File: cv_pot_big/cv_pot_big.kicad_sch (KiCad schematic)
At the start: 12 parts, among them J1 I/O connector, U1 HT7550-1, U2 LMV321IDBVR

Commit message: Switched to TLV6001UIDBVR Opamp
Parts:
- RV1: footprint cycfi_library:bourns_pdb181 -> cycfi_library:bourns_pdb241
- U2: value LMV321IDBVR -> TLV6001UIDBVR; LCSC C7972 -> (none)
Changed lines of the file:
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@@
       (effects (font (size 1.27 1.27)) (justify right))
     )
-    (property "Footprint" "cycfi_library:bourns_pdb181" (id 2) (at 88.9 101.6 0)
+    (property "Footprint" "cycfi_library:bourns_pdb241" (id 2) (at 88.9 101.6 0)
       (effects (font (size 1.27 1.27)) hide)
     )
@@
     (in_bom yes) (on_board yes)
     (property "Reference" "U2" (id 0) (at 153.67 96.52 0))
-    (property "Value" "LMV321IDBVR" (id 1) (at 153.67 99.0569 0))
+    (property "Value" "TLV6001UIDBVR" (id 1) (at 153.67 99.0569 0))
     (property "Footprint" "Package_TO_SOT_SMD:SOT-23-5" (id 2) (at 142.24 109.22 0)
       (effects (font (size 1.27 1.27)) (justify left) hide)
@@
     (property "Datasheet" "" (id 3) (at 144.78 99.06 0)
       (effects (font (size 1.27 1.27)) hide)
-    )
-    (property "LCSC" "C7972" (id 4) (at 144.78 104.14 0)
-      (effects (font (size 1.524 1.524)) hide)
     )
     (pin "2")
@@
     )
     (path "/9763309a-c9ed-492f-a4a9-0b6f407725b0"
-      (reference "RV1") (unit 1) (value "25k") (footprint "cycfi_library:bourns_pdb181")
+      (reference "RV1") (unit 1) (value "25k") (footprint "cycfi_library:bourns_pdb241")
     )
     (path "/b29e7a3c-8a61-4d5d-8478-053e45b60270"
@@
     )
     (path "/e69c64f9-717d-4a97-b3df-80325ec2fa63"
-      (reference "U2") (unit 1) (value "LMV321IDBVR") (footprint "Package_TO_SOT_SMD:SOT-23-5")
-    )
-  )
+      (reference "U2") (unit 1) (value "TLV6001UIDBVR") (footprint "Package_TO_SOT_SMD:SOT-23-5")
+    )
+  )

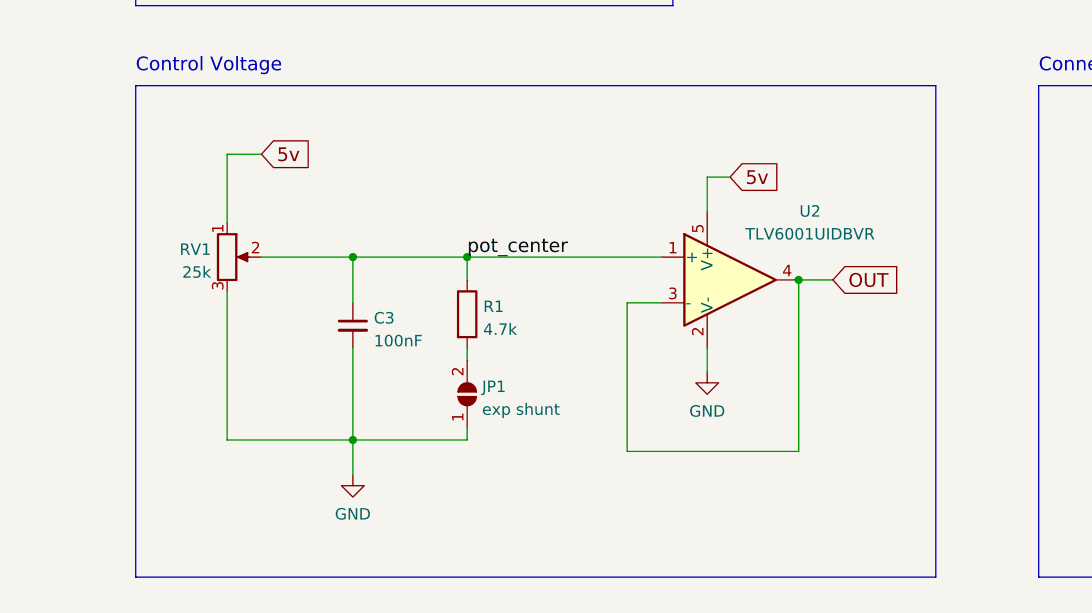
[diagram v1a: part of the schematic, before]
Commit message: Added 1k output resistor
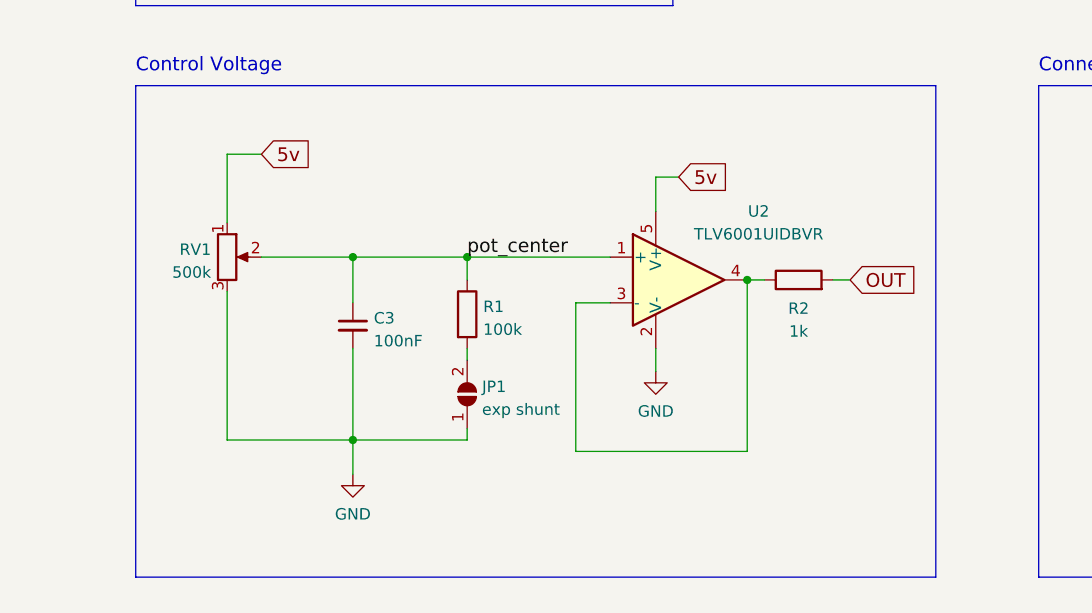
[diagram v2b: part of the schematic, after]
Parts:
- added R2: 1k, Resistor_SMD:R_0402_1005Metric, symbol Device:R
- R1: value 4.7k -> 100k; LCSC C25900 -> C25741
- RV1: value 25k -> 500k
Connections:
- net OUT: now also R2.2; no longer U2.3 (-), U2.4
- new net: R2.1, U2.3 (-), U2.4
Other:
- moved on the sheet: U2
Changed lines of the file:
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@@
   (junction (at 99.06 48.26) (diameter 0) (color 0 0 0 0)
   )
-  (junction (at 152.4 104.14) (diameter 0) (color 0 0 0 0)
-  )
   (junction (at 120.65 59.69) (diameter 0) (color 0 0 0 0)
   )
   (junction (at 102.87 101.6) (diameter 0) (color 0 0 0 0)
   )
+  (junction (at 146.685 104.14) (diameter 0) (color 0 0 0 0)
+  )
   (junction (at 102.87 121.92) (diameter 0) (color 0 0 0 0)
   )
@@
     (stroke (width 0) (type default) (color 0 0 0 0))
   )
-  (wire (pts (xy 133.35 123.19) (xy 152.4 123.19))
-    (stroke (width 0) (type default) (color 0 0 0 0))
-  )
-  (wire (pts (xy 152.4 104.14) (xy 152.4 123.19))
+  (wire (pts (xy 127.635 123.19) (xy 146.685 123.19))
+    (stroke (width 0) (type default) (color 0 0 0 0))
+  )
+  (wire (pts (xy 146.685 104.14) (xy 146.685 123.19))
     (stroke (width 0) (type default) (color 0 0 0 0))
   )
@@
     (stroke (width 0) (type default) (color 0 0 0 0))
   )
+  (wire (pts (xy 156.21 104.14) (xy 158.115 104.14))
+    (stroke (width 0) (type default) (color 0 0 0 0))
+  )
   (wire (pts (xy 92.71 101.6) (xy 102.87 101.6))
     (stroke (width 0) (type default) (color 0 0 0 0))
@@
     (stroke (width 0) (type default) (color 0 0 0 0))
   )
-  (wire (pts (xy 152.4 104.14) (xy 156.21 104.14))
-    (stroke (width 0) (type default) (color 0 0 0 0))
-  )
   (wire (pts (xy 120.65 59.69) (xy 124.46 59.69))
     (stroke (width 0) (type default) (color 0 0 0 0))
@@
     (stroke (width 0) (type default) (color 0 0 0 0))
   )
-  (wire (pts (xy 142.24 111.76) (xy 142.24 114.3))
+  (wire (pts (xy 136.525 111.76) (xy 136.525 114.3))
     (stroke (width 0) (type default) (color 0 0 0 0))
   )
@@
     (stroke (width 0) (type default) (color 0 0 0 0))
   )
-  (wire (pts (xy 142.24 92.71) (xy 144.78 92.71))
+  (wire (pts (xy 136.525 92.71) (xy 139.065 92.71))
     (stroke (width 0) (type default) (color 0 0 0 0))
   )
@@
     (stroke (width 0) (type default) (color 0 0 0 0))
   )
-  (wire (pts (xy 133.35 106.68) (xy 133.35 123.19))
-    (stroke (width 0) (type default) (color 0 0 0 0))
-  )
-  (wire (pts (xy 137.16 106.68) (xy 133.35 106.68))
+  (wire (pts (xy 146.685 104.14) (xy 148.59 104.14))
+    (stroke (width 0) (type default) (color 0 0 0 0))
+  )
+  (wire (pts (xy 127.635 106.68) (xy 127.635 123.19))
+    (stroke (width 0) (type default) (color 0 0 0 0))
+  )
+  (wire (pts (xy 131.445 106.68) (xy 127.635 106.68))
     (stroke (width 0) (type default) (color 0 0 0 0))
   )
@@
     (stroke (width 0) (type default) (color 0 0 0 0))
   )
-  (wire (pts (xy 142.24 96.52) (xy 142.24 92.71))
+  (wire (pts (xy 136.525 96.52) (xy 136.525 92.71))
     (stroke (width 0) (type default) (color 0 0 0 0))
   )
@@
     (stroke (width 0) (type default) (color 0 0 0 0))
   )
-  (wire (pts (xy 115.57 101.6) (xy 137.16 101.6))
+  (wire (pts (xy 115.57 101.6) (xy 131.445 101.6))
     (stroke (width 0) (type default) (color 0 0 0 0))
   )
@@
     )
   )
-  (global_label "5v" (shape input) (at 144.78 92.71 0) (fields_autoplaced)
+  (global_label "5v" (shape input) (at 139.065 92.71 0) (fields_autoplaced)
     (effects (font (size 1.524 1.524)) (justify left))
-    (property "Intersheet References" "${INTERSHEET_REFS}" (id 0) (at 150.1815 92.6148 0)
+    (property "Intersheet References" "${INTERSHEET_REFS}" (id 0) (at 144.4665 92.6148 0)
       (effects (font (size 1.524 1.524)) (justify left) hide)
     )
@@
     )
   )
-  (global_label "OUT" (shape input) (at 156.21 104.14 0) (fields_autoplaced)
+  (global_label "OUT" (shape input) (at 158.115 104.14 0) (fields_autoplaced)
     (effects (font (size 1.524 1.524)) (justify left))
-    (property "Intersheet References" "${INTERSHEET_REFS}" (id 0) (at 163.3532 104.0448 0)
+    (property "Intersheet References" "${INTERSHEET_REFS}" (id 0) (at 165.2582 104.0448 0)
       (effects (font (size 1.524 1.524)) (justify left) hide)
     )
@@
     (pin "1")
   )
-  (symbol (lib_id "power:GND") (at 142.24 114.3 0) (unit 1)
-    (in_bom yes) (on_board yes) (fields_autoplaced)
-    (property "Reference" "#PWR05" (id 0) (at 142.24 120.65 0)
-      (effects (font (size 1.27 1.27)) hide)
-    )
-    (property "Value" "GND" (id 1) (at 142.24 118.7434 0))
-    (property "Footprint" "" (id 2) (at 142.24 114.3 0)
-      (effects (font (size 1.27 1.27)) hide)
-    )
-    (property "Datasheet" "" (id 3) (at 142.24 114.3 0)
+  (symbol (lib_id "Device:R") (at 152.4 104.14 90) (unit 1)
+    (in_bom yes) (on_board yes)
+    (property "Reference" "R2" (id 0) (at 152.4 107.3181 90))
+    (property "Value" "1k" (id 1) (at 152.4 109.855 90))
+    (property "Footprint" "Resistor_SMD:R_0402_1005Metric" (id 2) (at 152.4 105.918 90)
+      (effects (font (size 1.27 1.27)) hide)
+    )
+    (property "Datasheet" "~" (id 3) (at 152.4 104.14 0)
+      (effects (font (size 1.27 1.27)) hide)
+    )
+    (property "LCSC" "C11702" (id 4) (at 152.4 104.14 0)
+      (effects (font (size 1.524 1.524)) hide)
+    )
+    (pin "1")
+    (pin "2")
+  )
+  (symbol (lib_id "power:GND") (at 136.525 114.3 0) (unit 1)
+    (in_bom yes) (on_board yes) (fields_autoplaced)
+    (property "Reference" "#PWR05" (id 0) (at 136.525 120.65 0)
+      (effects (font (size 1.27 1.27)) hide)
+    )
+    (property "Value" "GND" (id 1) (at 136.525 118.7434 0))
+    (property "Footprint" "" (id 2) (at 136.525 114.3 0)
+      (effects (font (size 1.27 1.27)) hide)
+    )
+    (property "Datasheet" "" (id 3) (at 136.525 114.3 0)
       (effects (font (size 1.27 1.27)) hide)
     )
@@
       (effects (font (size 1.27 1.27)) (justify left))
     )
-    (property "Value" "4.7k" (id 1) (at 117.348 109.6522 0)
+    (property "Value" "100k" (id 1) (at 117.348 109.6522 0)
       (effects (font (size 1.27 1.27)) (justify left))
     )
@@
       (effects (font (size 1.27 1.27)) hide)
     )
-    (property "LCSC" "C25900" (id 4) (at 115.57 107.95 0)
+    (property "LCSC" "C25741" (id 4) (at 115.57 107.95 0)
       (effects (font (size 1.524 1.524)) hide)
     )
@@
       (effects (font (size 1.27 1.27)) (justify right))
     )
-    (property "Value" "25k" (id 1) (at 87.1221 103.3022 0)
+    (property "Value" "500k" (id 1) (at 87.1221 103.3022 0)
       (effects (font (size 1.27 1.27)) (justify right))
     )
@@
     (pin "2")
   )
-  (symbol (lib_id "cycfi_library:opamp_dbv2") (at 144.78 104.14 0) (unit 1)
+  (symbol (lib_id "cycfi_library:opamp_dbv2") (at 139.065 104.14 0) (unit 1)
     (in_bom yes) (on_board yes)
-    (property "Reference" "U2" (id 0) (at 153.67 96.52 0))
-    (property "Value" "TLV6001UIDBVR" (id 1) (at 153.67 99.0569 0))
-    (property "Footprint" "Package_TO_SOT_SMD:SOT-23-5" (id 2) (at 142.24 109.22 0)
+    (property "Reference" "U2" (id 0) (at 147.955 96.52 0))
+    (property "Value" "TLV6001UIDBVR" (id 1) (at 147.955 99.0569 0))
+    (property "Footprint" "Package_TO_SOT_SMD:SOT-23-5" (id 2) (at 136.525 109.22 0)
       (effects (font (size 1.27 1.27)) (justify left) hide)
     )
-    (property "Datasheet" "" (id 3) (at 144.78 99.06 0)
+    (property "Datasheet" "" (id 3) (at 139.065 99.06 0)
       (effects (font (size 1.27 1.27)) hide)
     )
@@
     )
     (path "/7b3b0a10-97e8-4760-9212-cec2185ba7eb"
-      (reference "R1") (unit 1) (value "4.7k") (footprint "Resistor_SMD:R_0402_1005Metric")
+      (reference "R1") (unit 1) (value "100k") (footprint "Resistor_SMD:R_0402_1005Metric")
+    )
+    (path "/2e88006f-6a8c-4c9b-9825-22a6fc21ec72"
+      (reference "R2") (unit 1) (value "1k") (footprint "Resistor_SMD:R_0402_1005Metric")
     )
     (path "/9763309a-c9ed-492f-a4a9-0b6f407725b0"
-      (reference "RV1") (unit 1) (value "25k") (footprint "cycfi_library:bourns_pdb241")
+      (reference "RV1") (unit 1) (value "500k") (footprint "cycfi_library:bourns_pdb241")
     )
     (path "/b29e7a3c-8a61-4d5d-8478-053e45b60270"

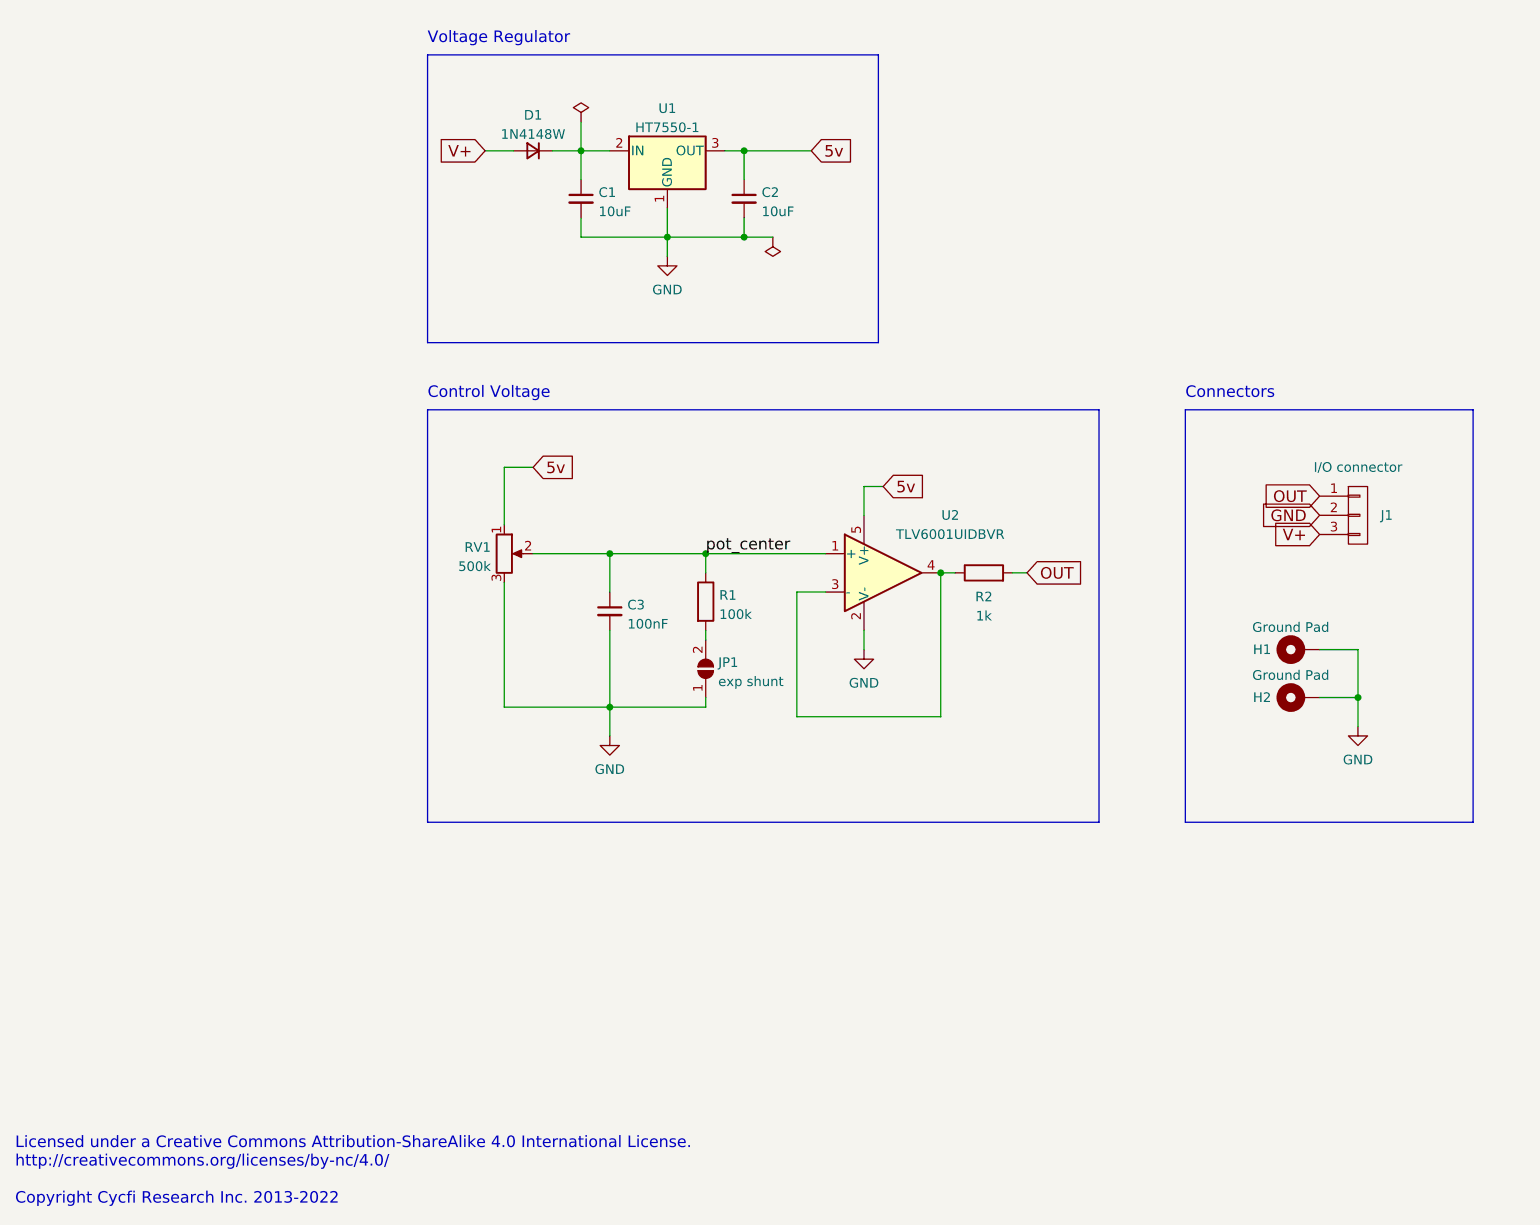
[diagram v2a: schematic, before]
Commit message: Big pot update: the header now points towards the terminals side
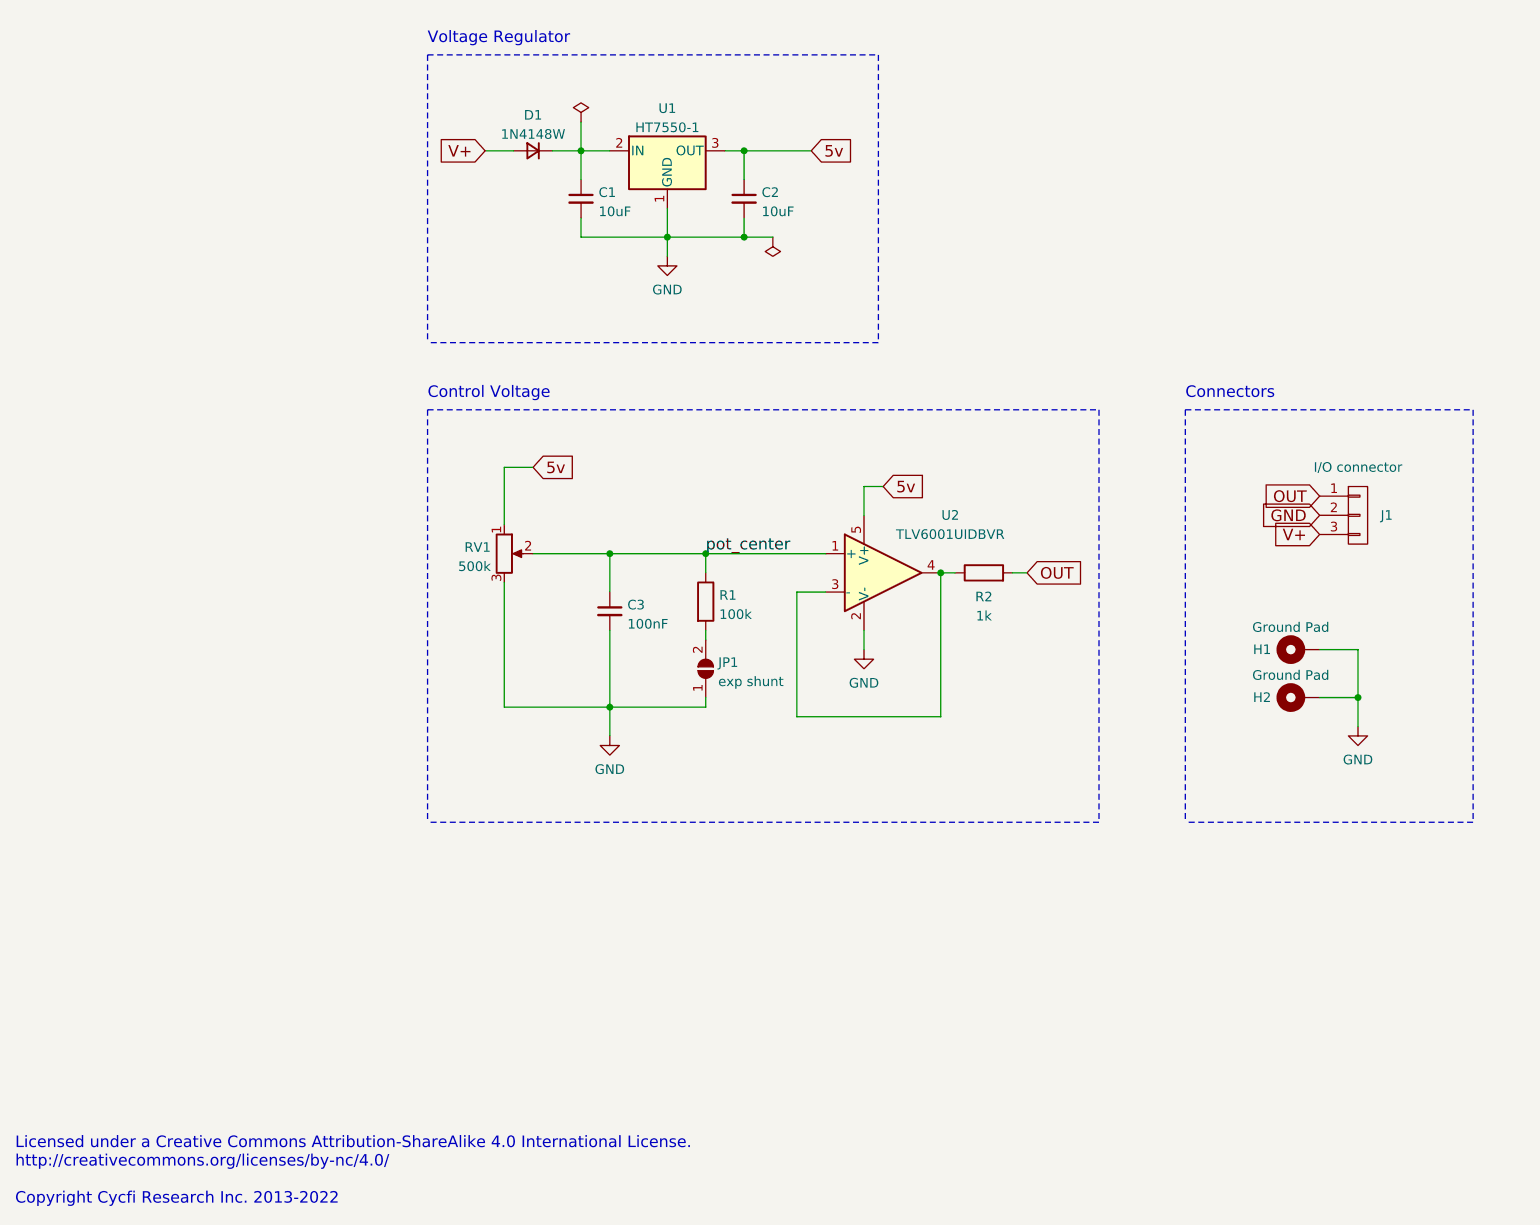
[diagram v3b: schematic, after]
